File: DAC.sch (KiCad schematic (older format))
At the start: 20 parts, among them U2 PCM5102, U3 AP1117-33

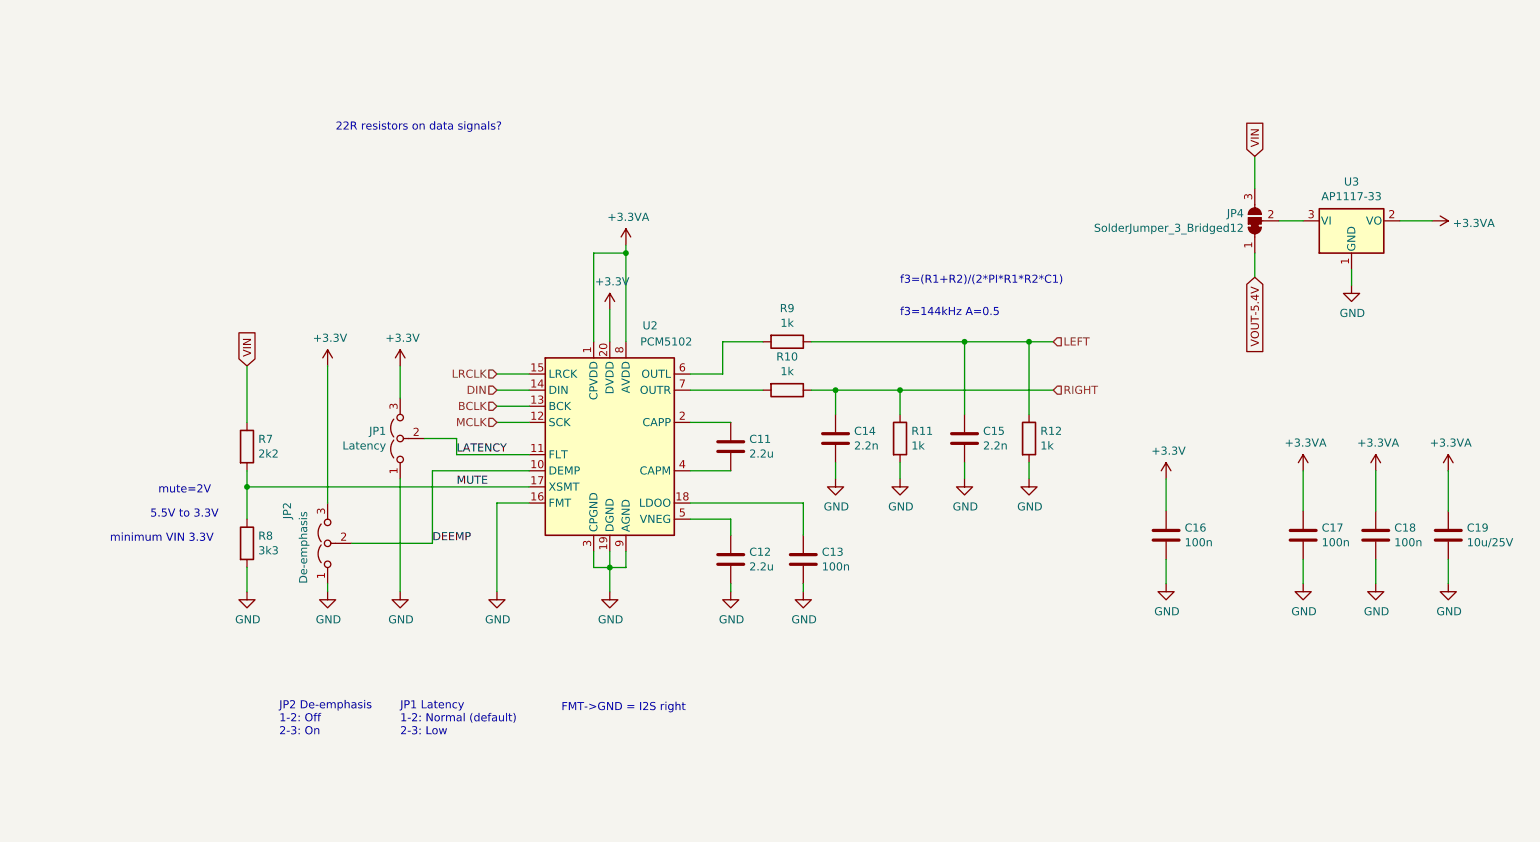
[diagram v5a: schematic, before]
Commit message: larger conn
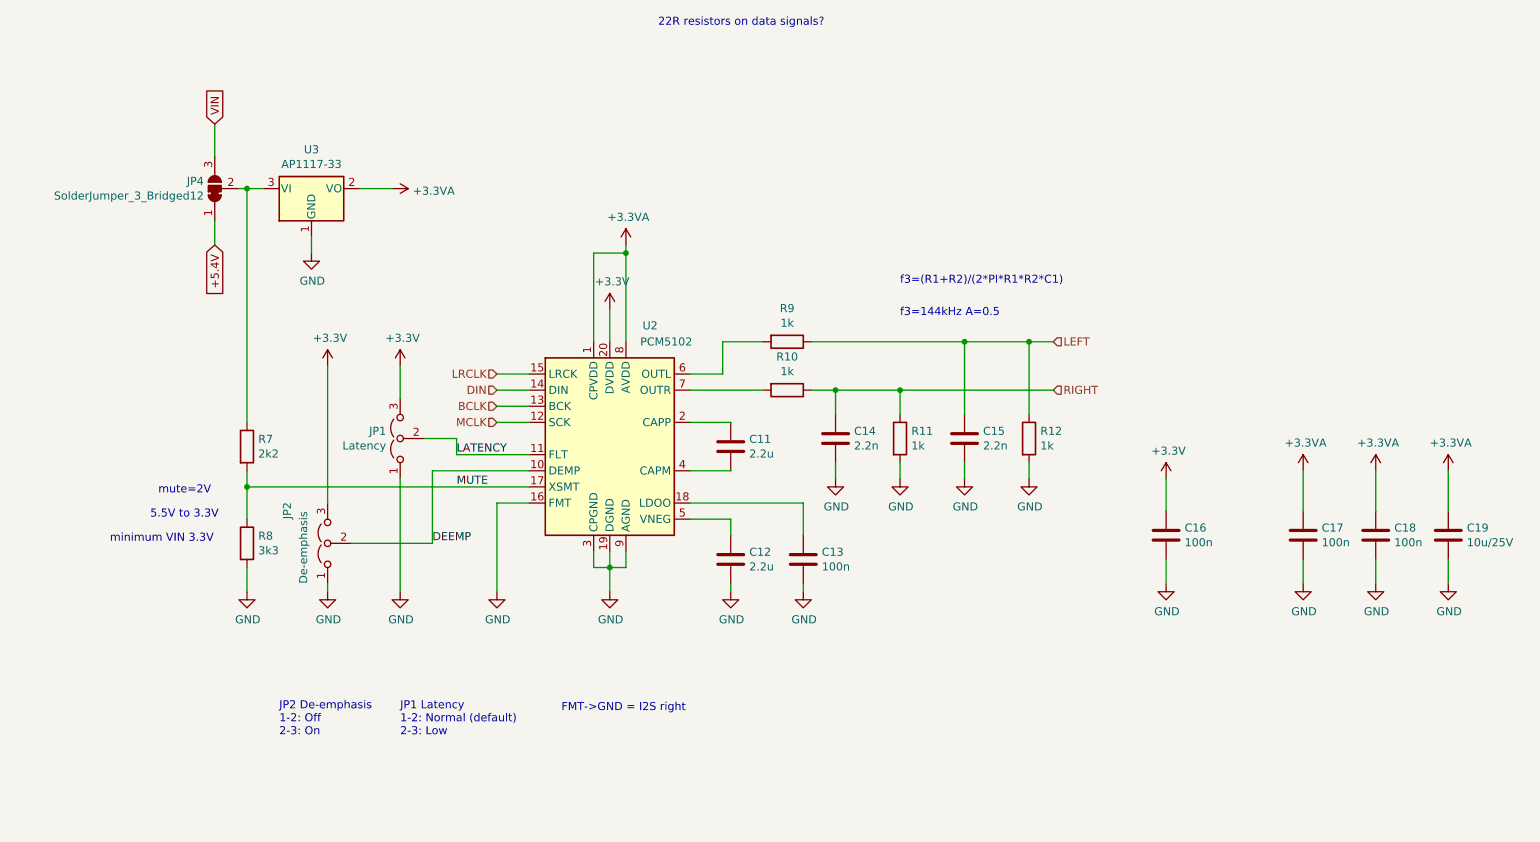
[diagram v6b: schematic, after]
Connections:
- net VIN: no longer R7.1
- net at JP4.2 (C), U3.3 (VI): now also R7.1
- net VOUT-5.4V renamed +5.4V
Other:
- moved on the sheet: JP4, U3
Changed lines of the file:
@@
 Wire Wire Line
 	3200 4650 3200 4500
-Wire Wire Line
-	3200 3600 3200 3250
-Text Notes 3750 1800 0    50   ~ 0
+Text Notes 5750 1150 0    50   ~ 0
 22R resistors on data signals?
 $Comp
@@
 Text Label 4500 3800 0    50   ~ 0
 LATENCY
-Text GLabel 3200 3250 1    50   Input ~ 0
-VIN
 Text Notes 2600 4200 0    50   ~ 0
 5.5V to 3.3V
@@
 L Regulator_Linear:AP1117-33 U3
 U 1 1 5D456577
-P 10050 2350
-F 0 "U3" H 10050 2592 50  0000 C CNN
-F 1 "AP1117-33" H 10050 2501 50  0000 C CNN
-F 2 "Package_TO_SOT_SMD:SOT-223-3_TabPin2" H 10050 2550 50  0001 C CNN
-F 3 "http://www.diodes.com/datasheets/AP1117.pdf" H 10150 2100 50  0001 C CNN
-	1    10050 2350
+P 3600 2150
+F 0 "U3" H 3600 2392 50  0000 C CNN
+F 1 "AP1117-33" H 3600 2301 50  0000 C CNN
+F 2 "Package_TO_SOT_SMD:SOT-223-3_TabPin2" H 3600 2350 50  0001 C CNN
+F 3 "http://www.diodes.com/datasheets/AP1117.pdf" H 3700 1900 50  0001 C CNN
+	1    3600 2150
 	1    0    0    -1
 $EndComp
@@
 L power:GND #PWR047
 U 1 1 5D457C9B
-P 10050 2750
-F 0 "#PWR047" H 10050 2500 50  0001 C CNN
-F 1 "GND" H 10055 2577 50  0000 C CNN
-F 2 "" H 10050 2750 50  0001 C CNN
-F 3 "" H 10050 2750 50  0001 C CNN
-	1    10050 2750
+P 3600 2550
+F 0 "#PWR047" H 3600 2300 50  0001 C CNN
+F 1 "GND" H 3605 2377 50  0000 C CNN
+F 2 "" H 3600 2550 50  0001 C CNN
+F 3 "" H 3600 2550 50  0001 C CNN
+	1    3600 2550
 	1    0    0    -1
 $EndComp
@@
 L power:+3.3VA #PWR079
 U 1 1 5D457FEA
-P 10550 2350
-F 0 "#PWR079" H 10550 2200 50  0001 C CNN
-F 1 "+3.3VA" V 10565 2478 50  0000 L CNN
-F 2 "" H 10550 2350 50  0001 C CNN
-F 3 "" H 10550 2350 50  0001 C CNN
-	1    10550 2350
+P 4100 2150
+F 0 "#PWR079" H 4100 2000 50  0001 C CNN
+F 1 "+3.3VA" V 4115 2278 50  0000 L CNN
+F 2 "" H 4100 2150 50  0001 C CNN
+F 3 "" H 4100 2150 50  0001 C CNN
+	1    4100 2150
 	0    1    1    0
 $EndComp
 Wire Wire Line
-	10050 2650 10050 2750
-Wire Wire Line
-	10350 2350 10550 2350
+	3600 2450 3600 2550
+Wire Wire Line
+	3900 2150 4100 2150
 Wire Wire Line
 	5350 3100 5350 2550
@@
 L Jumper:SolderJumper_3_Bridged12 JP4
 U 1 1 5D497685
-P 9450 2350
-F 0 "JP4" V 9496 2418 50  0000 L CNN
-F 1 "SolderJumper_3_Bridged12" V 9405 2418 50  0000 L CNN
-F 2 "Jumper:SolderJumper-3_P1.3mm_Bridged12_Pad1.0x1.5mm" H 9450 2350 50  0001 C CNN
-F 3 "~" H 9450 2350 50  0001 C CNN
-	1    9450 2350
+P 3000 2150
+F 0 "JP4" V 3046 2218 50  0000 L CNN
+F 1 "SolderJumper_3_Bridged12" V 2955 2218 50  0000 L CNN
+F 2 "Jumper:SolderJumper-3_P1.3mm_Bridged12_Pad1.0x1.5mm" H 3000 2150 50  0001 C CNN
+F 3 "~" H 3000 2150 50  0001 C CNN
+	1    3000 2150
 	0    -1   -1   0
 $EndComp
-Text GLabel 9450 1950 1    50   Input ~ 0
+Text GLabel 3000 1750 1    50   Input ~ 0
 VIN
 Wire Wire Line
-	9450 2150 9450 1950
-Wire Wire Line
-	9600 2350 9750 2350
-Text GLabel 9450 2700 3    50   Input ~ 0
-VOUT-5.4V
-Wire Wire Line
-	9450 2700 9450 2550
+	3000 1950 3000 1750
+Wire Wire Line
+	3150 2150 3200 2150
+Text GLabel 3000 2500 3    50   Input ~ 0
++5.4V
+Wire Wire Line
+	3000 2500 3000 2350
+Wire Wire Line
+	3200 3600 3200 2150
+Connection ~ 3200 2150
+Wire Wire Line
+	3200 2150 3300 2150
 $EndSCHEMATC

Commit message: sch improv
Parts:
- added C28: 100n, Capacitor_SMD:C_0402_1005Metric, symbol Device:C
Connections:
- net +3.3VA: now also C28.1
- net GND: now also C28.2
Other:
- moved on the sheet: C18
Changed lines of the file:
@@
 L Device:C C18
 U 1 1 5D42884D
-P 10200 4300
-F 0 "C18" H 10315 4346 50  0000 L CNN
-F 1 "100n" H 10315 4255 50  0000 L CNN
-F 2 "Capacitor_SMD:C_0402_1005Metric" H 10238 4150 50  0001 C CNN
-F 3 "~" H 10200 4300 50  0001 C CNN
-	1    10200 4300
+P 8900 5600
+F 0 "C18" H 9015 5646 50  0000 L CNN
+F 1 "100n" H 9015 5555 50  0000 L CNN
+F 2 "Capacitor_SMD:C_0402_1005Metric" H 8938 5450 50  0001 C CNN
+F 3 "~" H 8900 5600 50  0001 C CNN
+	1    8900 5600
 	1    0    0    -1
 $EndComp
@@
 L power:GND #PWR046
 U 1 1 5D42B3EB
-P 10200 4600
-F 0 "#PWR046" H 10200 4350 50  0001 C CNN
-F 1 "GND" H 10205 4427 50  0000 C CNN
-F 2 "" H 10200 4600 50  0001 C CNN
-F 3 "" H 10200 4600 50  0001 C CNN
-	1    10200 4600
+P 8900 5900
+F 0 "#PWR046" H 8900 5650 50  0001 C CNN
+F 1 "GND" H 8905 5727 50  0000 C CNN
+F 2 "" H 8900 5900 50  0001 C CNN
+F 3 "" H 8900 5900 50  0001 C CNN
+	1    8900 5900
 	1    0    0    -1
 $EndComp
@@
 	9750 4600 9750 4450
 Wire Wire Line
-	10200 4600 10200 4450
+	8900 5900 8900 5750
 Wire Wire Line
 	8900 4150 8900 3950
@@
 L power:+3.3VA #PWR078
 U 1 1 5D44C719
-P 10200 3900
-F 0 "#PWR078" H 10200 3750 50  0001 C CNN
-F 1 "+3.3VA" H 10215 4073 50  0000 C CNN
-F 2 "" H 10200 3900 50  0001 C CNN
-F 3 "" H 10200 3900 50  0001 C CNN
-	1    10200 3900
-	1    0    0    -1
-$EndComp
-Wire Wire Line
-	10200 3900 10200 4150
+P 8900 5200
+F 0 "#PWR078" H 8900 5050 50  0001 C CNN
+F 1 "+3.3VA" H 8915 5373 50  0000 C CNN
+F 2 "" H 8900 5200 50  0001 C CNN
+F 3 "" H 8900 5200 50  0001 C CNN
+	1    8900 5200
+	1    0    0    -1
+$EndComp
+Wire Wire Line
+	8900 5200 8900 5450
 Wire Wire Line
 	10650 3900 10650 4150
@@
 L power:GND #PWR047
 U 1 1 5D457C9B
-P 3600 2550
-F 0 "#PWR047" H 3600 2300 50  0001 C CNN
-F 1 "GND" H 3605 2377 50  0000 C CNN
-F 2 "" H 3600 2550 50  0001 C CNN
-F 3 "" H 3600 2550 50  0001 C CNN
-	1    3600 2550
+P 3600 2600
+F 0 "#PWR047" H 3600 2350 50  0001 C CNN
+F 1 "GND" H 3605 2427 50  0000 C CNN
+F 2 "" H 3600 2600 50  0001 C CNN
+F 3 "" H 3600 2600 50  0001 C CNN
+	1    3600 2600
 	1    0    0    -1
 $EndComp
@@
 $EndComp
 Wire Wire Line
-	3600 2450 3600 2550
-Wire Wire Line
-	3900 2150 4100 2150
+	3600 2450 3600 2600
+Wire Wire Line
+	3900 2150 4000 2150
 Wire Wire Line
 	5350 3100 5350 2550
@@
 Wire Wire Line
 	3200 2150 3300 2150
+$Comp
+L Device:C C28
+U 1 1 5DE38FE5
+P 4000 2300
+F 0 "C28" H 4115 2346 50  0000 L CNN
+F 1 "100n" H 4115 2255 50  0000 L CNN
+F 2 "Capacitor_SMD:C_0402_1005Metric" H 4038 2150 50  0001 C CNN
+F 3 "~" H 4000 2300 50  0001 C CNN
+	1    4000 2300
+	1    0    0    -1
+$EndComp
+$Comp
+L power:GND #PWR043
+U 1 1 5DE38FEB
+P 4000 2600
+F 0 "#PWR043" H 4000 2350 50  0001 C CNN
+F 1 "GND" H 4005 2427 50  0000 C CNN
+F 2 "" H 4000 2600 50  0001 C CNN
+F 3 "" H 4000 2600 50  0001 C CNN
+	1    4000 2600
+	1    0    0    -1
+$EndComp
+Wire Wire Line
+	4000 2600 4000 2450
+Connection ~ 4000 2150
+Wire Wire Line
+	4000 2150 4100 2150
 $EndSCHEMATC

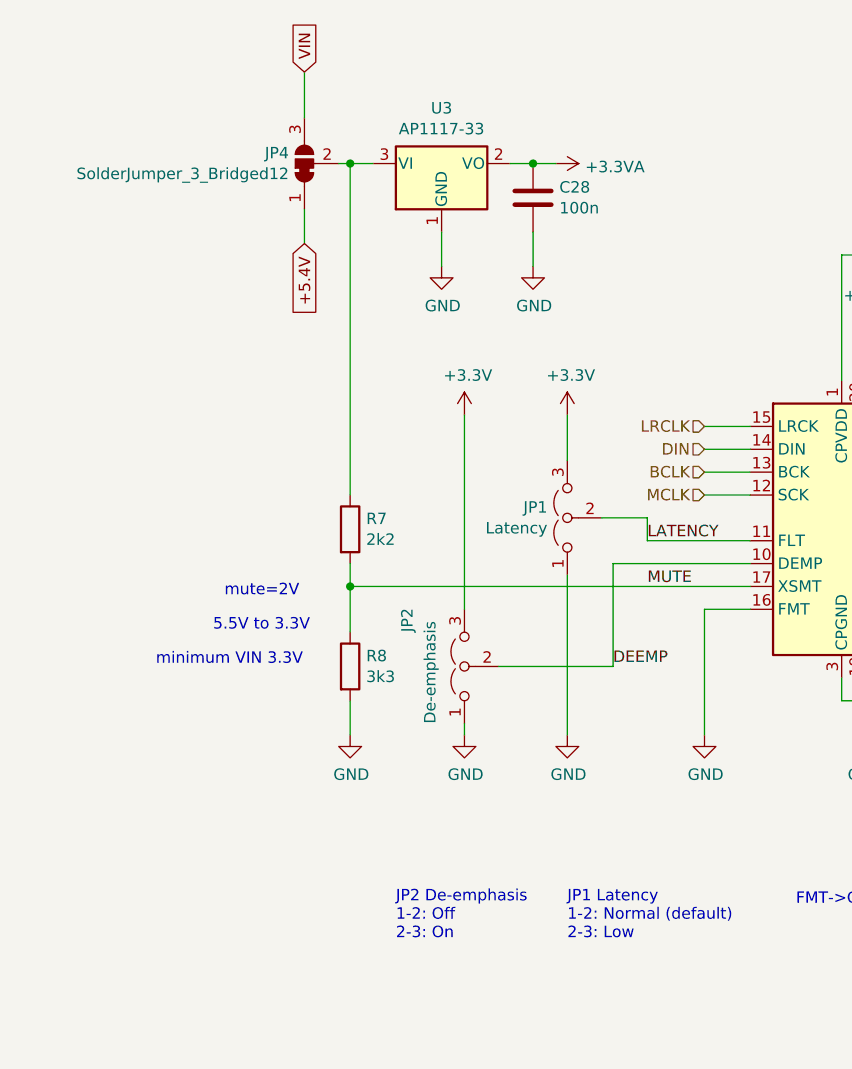
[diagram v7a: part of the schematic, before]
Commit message: smaller package, drc
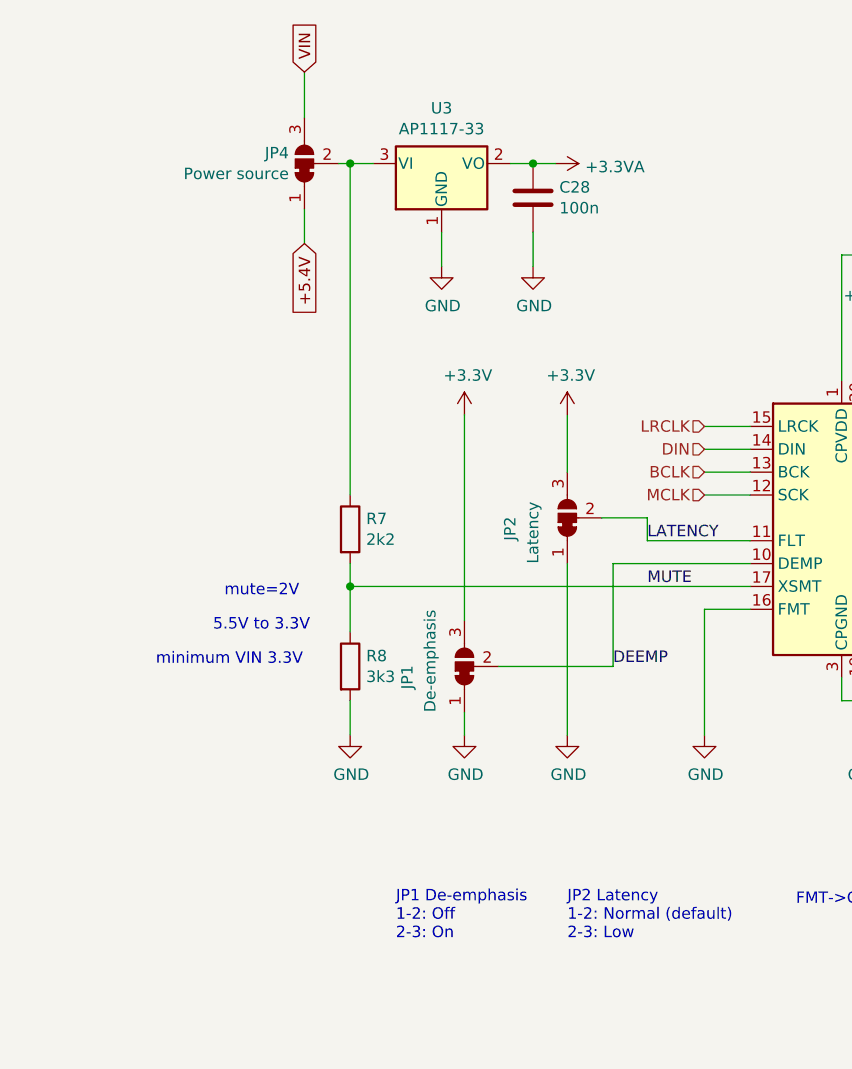
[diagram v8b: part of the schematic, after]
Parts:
- removed JP1: Latency, Connector_PinHeader_2.54mm:PinHeader_1x03_P2.54mm_Vertical, symbol Jumper:Jumper_3_Open
- removed JP2: De-emphasis, Connector_PinHeader_2.54mm:PinHeader_1x03_P2.54mm_Vertical, symbol Jumper:Jumper_3_Open
- added JP1: De-emphasis, Jumper:SolderJumper-3_P1.3mm_Bridged12_Pad1.0x1.5mm, symbol Jumper:SolderJumper_3_Bridged12
- added JP2: Latency, Jumper:SolderJumper-3_P1.3mm_Bridged12_Pad1.0x1.5mm, symbol Jumper:SolderJumper_3_Bridged12
- JP4: value SolderJumper_3_Bridged12 -> Power source
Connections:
- net +3V3: now also JP1.3 (B), JP2.3 (B)
- net DEEMP: now also JP1.2 (C)
- net GND: now also JP1.1 (A), JP2.1 (A)
- net LATENCY: now also JP2.2 (C)
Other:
- note added: "JP1 De-emphasis\n1-2: Off\n2-3: On"
- note added: "JP2 Latency\n1-2: Normal (default)\n2-3: Low\n"
- note removed: "JP1 Latency\n1-2: Normal (default)\n2-3: Low\n"
- note removed: "JP2 De-emphasis\n1-2: Off\n2-3: On"
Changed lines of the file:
@@
 22R resistors on data signals?
-$Comp
-L Jumper:Jumper_3_Open JP1
-U 1 1 5D45825E
-P 4150 3700
-F 0 "JP1" V 4196 3787 50  0000 L CNN
-F 1 "Latency" V 4105 3787 50  0000 L CNN
-F 2 "Connector_PinHeader_2.54mm:PinHeader_1x03_P2.54mm_Vertical" H 4150 3700 50  0001 C CNN
-F 3 "~" H 4150 3700 50  0001 C CNN
-	1    4150 3700
-	0    -1   -1   0
-$EndComp
-$Comp
-L Jumper:Jumper_3_Open JP2
-U 1 1 5D45BA3C
-P 3700 4350
-F 0 "JP2" H 3850 4600 50  0000 L CNN
-F 1 "De-emphasis" H 3450 4500 50  0000 L CNN
-F 2 "Connector_PinHeader_2.54mm:PinHeader_1x03_P2.54mm_Vertical" H 3700 4350 50  0001 C CNN
-F 3 "~" H 3700 4350 50  0001 C CNN
-	1    3700 4350
-	0    -1   -1   0
-$EndComp
 $Comp
 L power:+3.3V #PWR033
@@
 	1    0    0    -1
 $EndComp
-Wire Wire Line
-	3700 4100 3700 3250
-Wire Wire Line
-	4150 3450 4150 3250
 $Comp
 L power:GND #PWR029
@@
 	1    0    0    -1
 $EndComp
-Wire Wire Line
-	4150 4650 4150 3950
-Wire Wire Line
-	3700 4650 3700 4600
 Text Notes 4150 5550 0    50   ~ 0
-JP1 Latency\n1-2: Normal (default)\n2-3: Low\n
+JP2 Latency\n1-2: Normal (default)\n2-3: Low\n
 Text Notes 3400 5550 0    50   ~ 0
-JP2 De-emphasis\n1-2: Off\n2-3: On
+JP1 De-emphasis\n1-2: Off\n2-3: On
 Text Notes 7250 2750 0    50   ~ 0
 f3=(R1+R2)/(2*PI*R1*R2*C1)
@@
 	10650 3900 10650 4150
 $Comp
-L Regulator_Linear:AP1117-33 U3
-U 1 1 5D456577
-P 3600 2150
-F 0 "U3" H 3600 2392 50  0000 C CNN
-F 1 "AP1117-33" H 3600 2301 50  0000 C CNN
-F 2 "Package_TO_SOT_SMD:SOT-223-3_TabPin2" H 3600 2350 50  0001 C CNN
-F 3 "http://www.diodes.com/datasheets/AP1117.pdf" H 3700 1900 50  0001 C CNN
-	1    3600 2150
-	1    0    0    -1
-$EndComp
-$Comp
 L power:GND #PWR047
 U 1 1 5D457C9B
@@
 P 3000 2150
 F 0 "JP4" V 3046 2218 50  0000 L CNN
-F 1 "SolderJumper_3_Bridged12" V 2955 2218 50  0000 L CNN
+F 1 "Power source" V 2955 2218 50  0000 L CNN
 F 2 "Jumper:SolderJumper-3_P1.3mm_Bridged12_Pad1.0x1.5mm" H 3000 2150 50  0001 C CNN
 F 3 "~" H 3000 2150 50  0001 C CNN
@@
 Wire Wire Line
 	4000 2150 4100 2150
+$Comp
+L Jumper:SolderJumper_3_Bridged12 JP?
+U 1 1 5DDBF282
+P 4150 3700
+AR Path="/5DDBF282" Ref="JP?"  Part="1"
+AR Path="/5D41DA57/5DDBF282" Ref="JP2"  Part="1"
+F 0 "JP2" H 4050 3950 50  0000 L CNN
+F 1 "Latency" H 3950 3850 50  0000 L CNN
+F 2 "Jumper:SolderJumper-3_P1.3mm_Bridged12_Pad1.0x1.5mm" H 4150 3700 50  0001 C CNN
+F 3 "~" H 4150 3700 50  0001 C CNN
+	1    4150 3700
+	0    -1   -1   0
+$EndComp
+$Comp
+L Jumper:SolderJumper_3_Bridged12 JP?
+U 1 1 5DDC0F99
+P 3700 4350
+AR Path="/5DDC0F99" Ref="JP?"  Part="1"
+AR Path="/5D41DA57/5DDC0F99" Ref="JP1"  Part="1"
+F 0 "JP1" H 3600 4600 50  0000 L CNN
+F 1 "De-emphasis" H 3500 4500 50  0000 L CNN
+F 2 "Jumper:SolderJumper-3_P1.3mm_Bridged12_Pad1.0x1.5mm" H 3700 4350 50  0001 C CNN
+F 3 "~" H 3700 4350 50  0001 C CNN
+	1    3700 4350
+	0    -1   -1   0
+$EndComp
+Wire Wire Line
+	3700 3250 3700 4150
+Wire Wire Line
+	3700 4550 3700 4650
+Wire Wire Line
+	4150 3900 4150 4650
+Wire Wire Line
+	4150 3250 4150 3500
+$Comp
+L Regulator_Linear:AP1117-33 U3
+U 1 1 5D456577
+P 3600 2150
+F 0 "U3" H 3600 2392 50  0000 C CNN
+F 1 "AP1117-33" H 3600 2301 50  0000 C CNN
+F 2 "Package_TO_SOT_SMD:SOT-223-3_TabPin2" H 3600 2350 50  0001 C CNN
+F 3 "http://www.diodes.com/datasheets/AP1117.pdf" H 3700 1900 50  0001 C CNN
+	1    3600 2150
+	1    0    0    -1
+$EndComp
 $EndSCHEMATC
